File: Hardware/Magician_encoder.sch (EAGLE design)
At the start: 24 parts, among them U1 QRE1113, U2 QRE1113

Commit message: Changed opamp part number to U3
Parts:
- renumbered U$1 to U3
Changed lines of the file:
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@@
 <part name="R1" library="SparkFun-Resistors" deviceset="10KOHM1/10W1%(0603)" device="" value="10k"/>
 <part name="R2" library="SparkFun-Resistors" deviceset="1K-1%" device="" value="1k"/>
-<part name="U$1" library="SparkFun-AnalogIC" deviceset="LMV358" device=""/>
+<part name="U3" library="SparkFun-AnalogIC" deviceset="LMV358" device=""/>
 <part name="U2" library="SparkFun-Sensors" deviceset="QRE1113" device=""/>
 <part name="D1" library="SparkFun-DiscreteSemi" deviceset="RB751" device="" value="RB751"/>
@@
 <instance part="R1" gate="G$1" x="104.14" y="121.92"/>
 <instance part="R2" gate="G$1" x="86.36" y="121.92" rot="R180"/>
-<instance part="U$1" gate="G$1" x="104.14" y="104.14"/>
-<instance part="U$1" gate="G$2" x="200.66" y="104.14"/>
+<instance part="U3" gate="G$1" x="104.14" y="104.14"/>
+<instance part="U3" gate="G$2" x="200.66" y="104.14"/>
 <instance part="U2" gate="G$1" x="48.26" y="109.22" smashed="yes" rot="MR0">
 <attribute name="VALUE" x="50.038" y="112.268" size="1.778" layer="96" rot="MR0"/>
@@
 <segment>
 <pinref part="SUPPLY2" gate="G$1" pin="5V"/>
-<pinref part="U$1" gate="G$1" pin="+V"/>
+<pinref part="U3" gate="G$1" pin="+V"/>
 <wire x1="104.14" y1="111.76" x2="104.14" y2="109.22" width="0.1524" layer="91"/>
 </segment>
@@
 <segment>
 <pinref part="GND2" gate="1" pin="GND"/>
-<pinref part="U$1" gate="G$1" pin="GND"/>
+<pinref part="U3" gate="G$1" pin="GND"/>
 <wire x1="104.14" y1="96.52" x2="104.14" y2="99.06" width="0.1524" layer="91"/>
 </segment>
@@
 <net name="N$1" class="0">
 <segment>
-<pinref part="U$1" gate="G$1" pin="-IN1"/>
+<pinref part="U3" gate="G$1" pin="-IN1"/>
 <wire x1="93.98" y1="106.68" x2="96.52" y2="106.68" width="0.1524" layer="91"/>
 <wire x1="93.98" y1="106.68" x2="93.98" y2="121.92" width="0.1524" layer="91"/>
@@
 <wire x1="109.22" y1="121.92" x2="114.3" y2="121.92" width="0.1524" layer="91"/>
 <wire x1="114.3" y1="121.92" x2="114.3" y2="104.14" width="0.1524" layer="91"/>
-<pinref part="U$1" gate="G$1" pin="OUT1"/>
+<pinref part="U3" gate="G$1" pin="OUT1"/>
 <wire x1="114.3" y1="104.14" x2="111.76" y2="104.14" width="0.1524" layer="91"/>
 <label x="119.38" y="104.14" size="1.778" layer="95" xref="yes"/>
@@
 <net name="N$6" class="0">
 <segment>
-<pinref part="U$1" gate="G$1" pin="+IN1"/>
+<pinref part="U3" gate="G$1" pin="+IN1"/>
 <pinref part="D1" gate="G$1" pin="C"/>
 <wire x1="68.58" y1="99.06" x2="63.5" y2="99.06" width="0.1524" layer="91"/>
@@
 <wire x1="190.5" y1="121.92" x2="187.96" y2="121.92" width="0.1524" layer="91"/>
 <junction x="190.5" y="121.92"/>
-<pinref part="U$1" gate="G$2" pin="-IN2"/>
+<pinref part="U3" gate="G$2" pin="-IN2"/>
 <wire x1="190.5" y1="106.68" x2="193.04" y2="106.68" width="0.1524" layer="91"/>
 </segment>
@@
 <label x="215.9" y="104.14" size="1.778" layer="95" xref="yes"/>
 <wire x1="210.82" y1="104.14" x2="215.9" y2="104.14" width="0.1524" layer="91"/>
-<pinref part="U$1" gate="G$2" pin="OUT2"/>
+<pinref part="U3" gate="G$2" pin="OUT2"/>
 <wire x1="208.28" y1="104.14" x2="210.82" y2="104.14" width="0.1524" layer="91"/>
 <junction x="210.82" y="104.14"/>
@@
 <wire x1="193.04" y1="101.6" x2="160.02" y2="101.6" width="0.1524" layer="91"/>
 <junction x="160.02" y="101.6"/>
-<pinref part="U$1" gate="G$2" pin="+IN2"/>
-</segment>
-</net>
+<pinref part="U3" gate="G$2" pin="+IN2"/>
+</segment>
+</net>

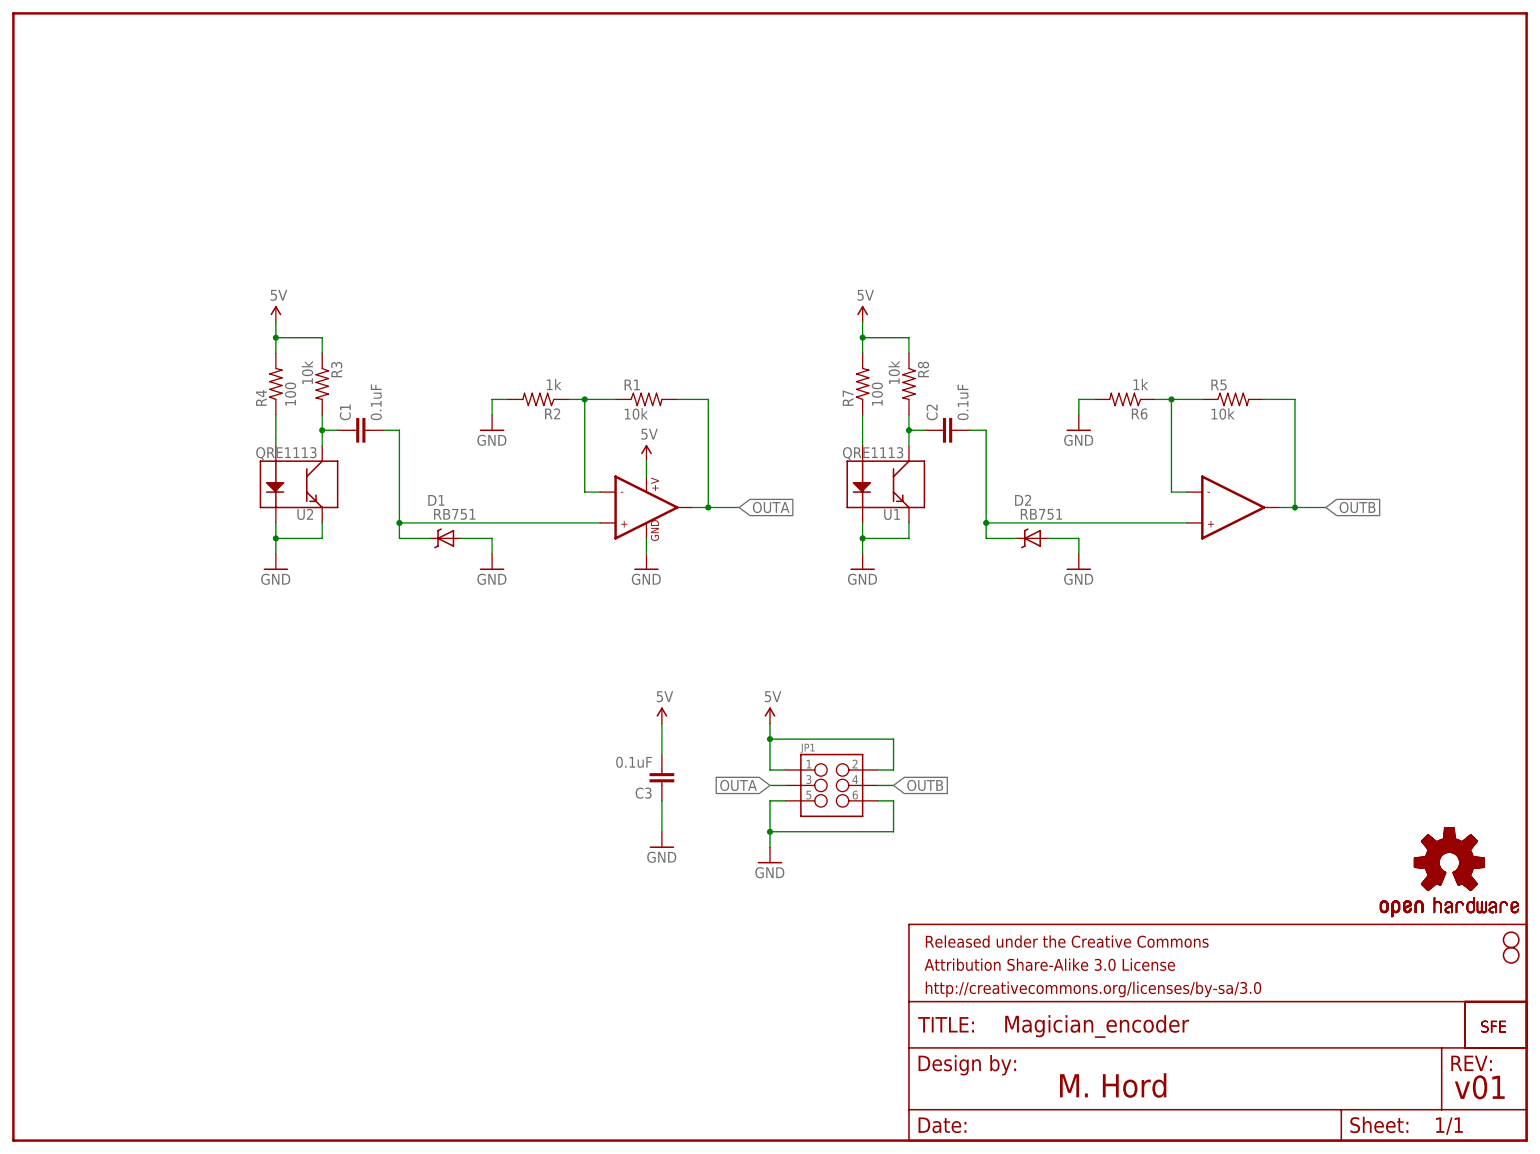
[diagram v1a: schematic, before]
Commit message: Total overhaul to BJT based circuit.
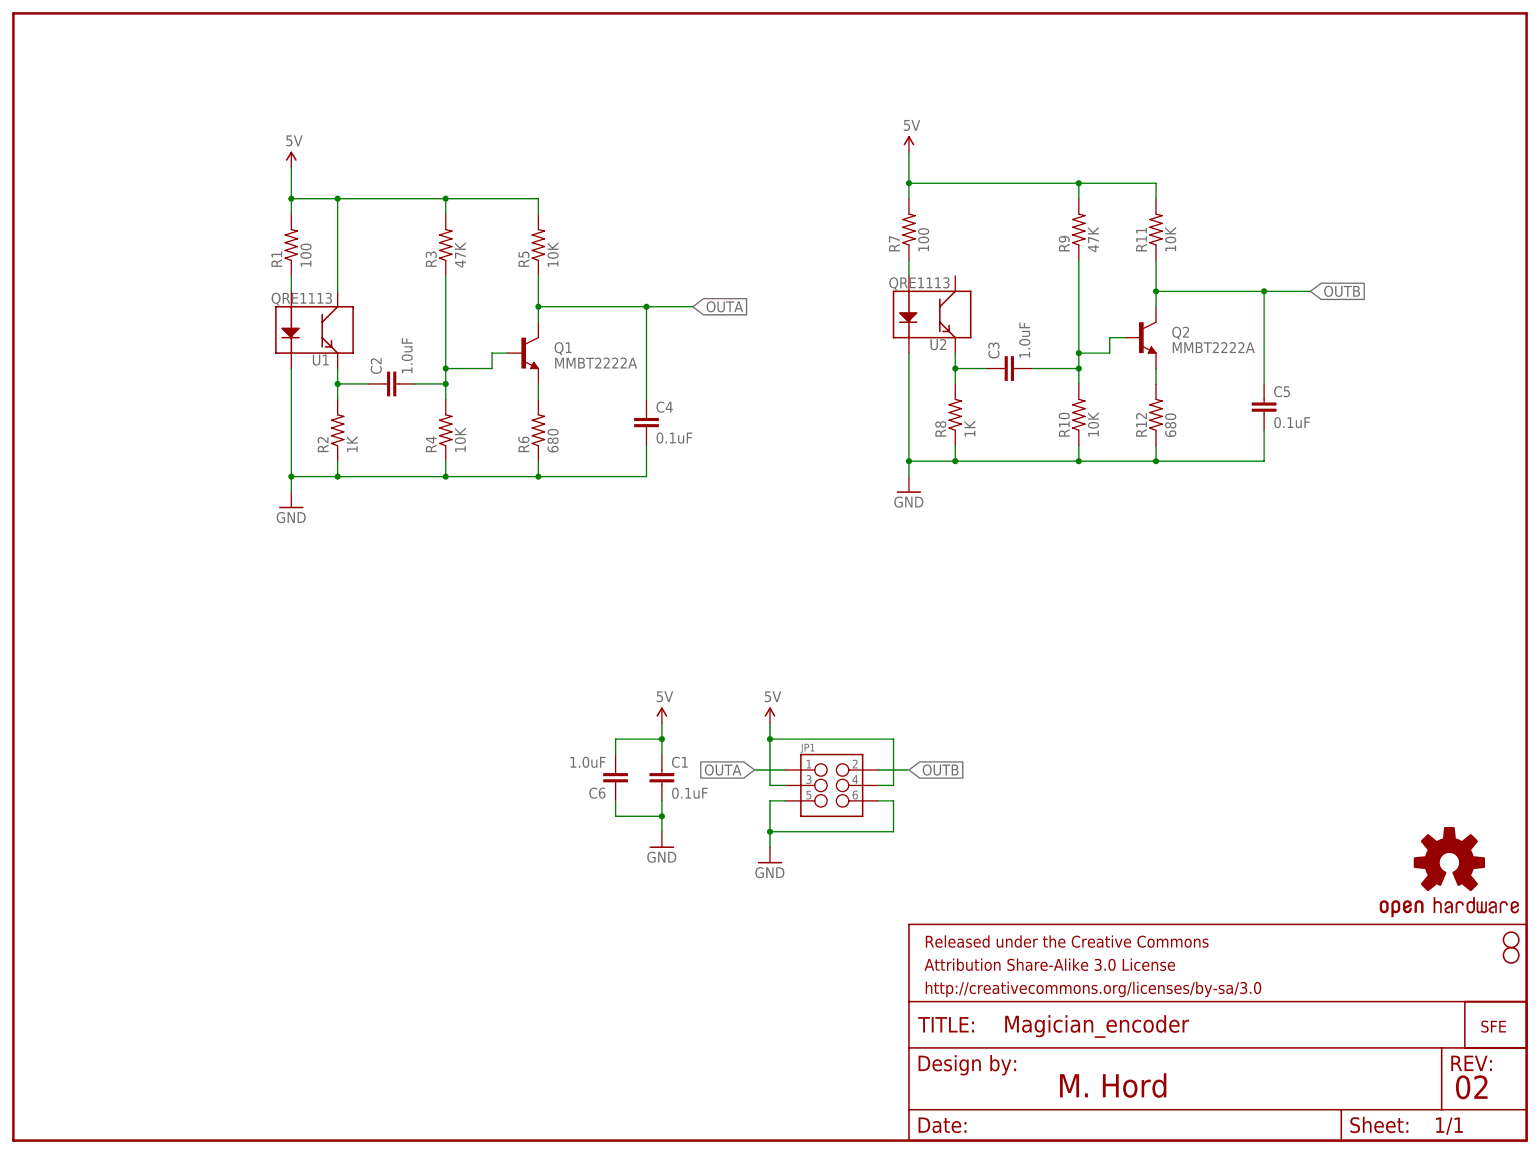
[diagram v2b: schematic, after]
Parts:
- removed D1, D2: RB751, SparkFun-DiscreteSemi:RB751
- removed LOGO1: LOGO-SFENEW, SparkFun-Aesthetics:LOGO-SFENEW
- removed LOGO2: OSHW-LOGOS, SparkFun-Aesthetics:OSHW-LOGOS
- removed U3: LMV358, SparkFun-AnalogIC:LMV358
- added C4, C5: 0.1uF, SparkFun-Capacitors:0.1UF-25V(+80/-20%)(0603)
- added C6: 1.0uF, SparkFun-Capacitors:1.0UF-16V-10%(0603)
- added Q1, Q2: MMBT2222A, SparkFun-DiscreteSemi:TRANSISTOR_NPNMMBT2222A
- added R10, R11: 10K, SparkFun-Resistors:10KOHM1/10W1%(0603)0603
- added R12: 680, SparkFun-Resistors:680OHM1/10W5%(0603)
- added R9: 47K, SparkFun-Resistors:47KOHM1/10W1%(0603)
- C2, C3: value 0.1uF -> 1.0uF; device SparkFun-Capacitors:0.1UF-25V(+80/-20%)(0603) -> SparkFun-Capacitors:1.0UF-16V-10%(0603)
- R1: value 10k -> 100; device SparkFun-Resistors:10KOHM1/10W1%(0603) -> SparkFun-Resistors:100OHM1/10W1%(0603)
- R2: value 1k -> 1K; device SparkFun-Resistors:1K-1% -> SparkFun-Resistors:1KOHM1/10W1%(0603)
- R3: value 10k -> 47K; device SparkFun-Resistors:10KOHM1/10W1%(0603) -> SparkFun-Resistors:47KOHM1/10W1%(0603)
- R4: value 100 -> 10K; device SparkFun-Resistors:100-1% -> SparkFun-Resistors:10KOHM1/10W1%(0603)0603
- R5: value 10k -> 10K; device SparkFun-Resistors:10KOHM1/10W1%(0603) -> SparkFun-Resistors:10KOHM1/10W1%(0603)0603
- R6: value 1k -> 680; device SparkFun-Resistors:1K-1% -> SparkFun-Resistors:680OHM1/10W5%(0603)
- R7: device SparkFun-Resistors:100-1% -> SparkFun-Resistors:100OHM1/10W1%(0603)
- R8: value 10k -> 1K; device SparkFun-Resistors:10KOHM1/10W1%(0603) -> SparkFun-Resistors:1KOHM1/10W1%(0603)
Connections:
- removed net N$11: C2.2, D2.C, U3G$2.+IN2
- removed net N$4: R5.1, R6.1, U3G$2.-IN2
- removed net N$6: C1.2, D1.C, U3G$1.+IN1
- new net N$2: C2.2, Q1.B, R3.1, R4.2
- new net N$7: Q2.E, R12.2
- new net N$8: C3.1, R8.2, U2.E
- net 5V: now also C1.1, C6.2, JP1.3, JP1.4, R1.2, R11.2, R3.2, R5.2, R9.2, U1.C; no longer C3.2, JP1.1, JP1.2, R3.1, R4.2, R8.1, U3G$1.+V
- net GND: now also C1.2, C4.2, C5.2, C6.1, R10.1, R12.1, R2.1, R4.1, R6.1, R8.1; no longer C3.1, D1.A, D2.A, R2.2, R6.2, U1.E, U2.E, U3G$1.GND
- net N$1: now also C2.1, R2.2, U1.E; no longer R1.1, R2.1, U3G$1.-IN1
- net N$10: now also U2.A; no longer U1.A
- net N$3: now also Q1.E, R6.2; no longer C1.1, R3.2, U2.C
- net N$5: now also R1.1, U1.A; no longer R4.1, U2.A
- net N$9: now also C3.2, Q2.B, R10.2, R9.1; no longer C2.1, R8.2, U1.C
- net OUTA: now also C4.1, JP1.1, Q1.C, R5.1; no longer JP1.3, R1.2, U3G$1.OUT1
- net OUTB: now also C5.1, JP1.2, Q2.C, R11.1; no longer JP1.4, R5.2, U3G$2.OUT2
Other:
- note added: "02"
- note removed: "v01"
- moved on the sheet: C1, C2, C3, R1, R2, R3, R4, R5, R6, R7, R8, U1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

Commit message: Change to discrete BJT circuit.
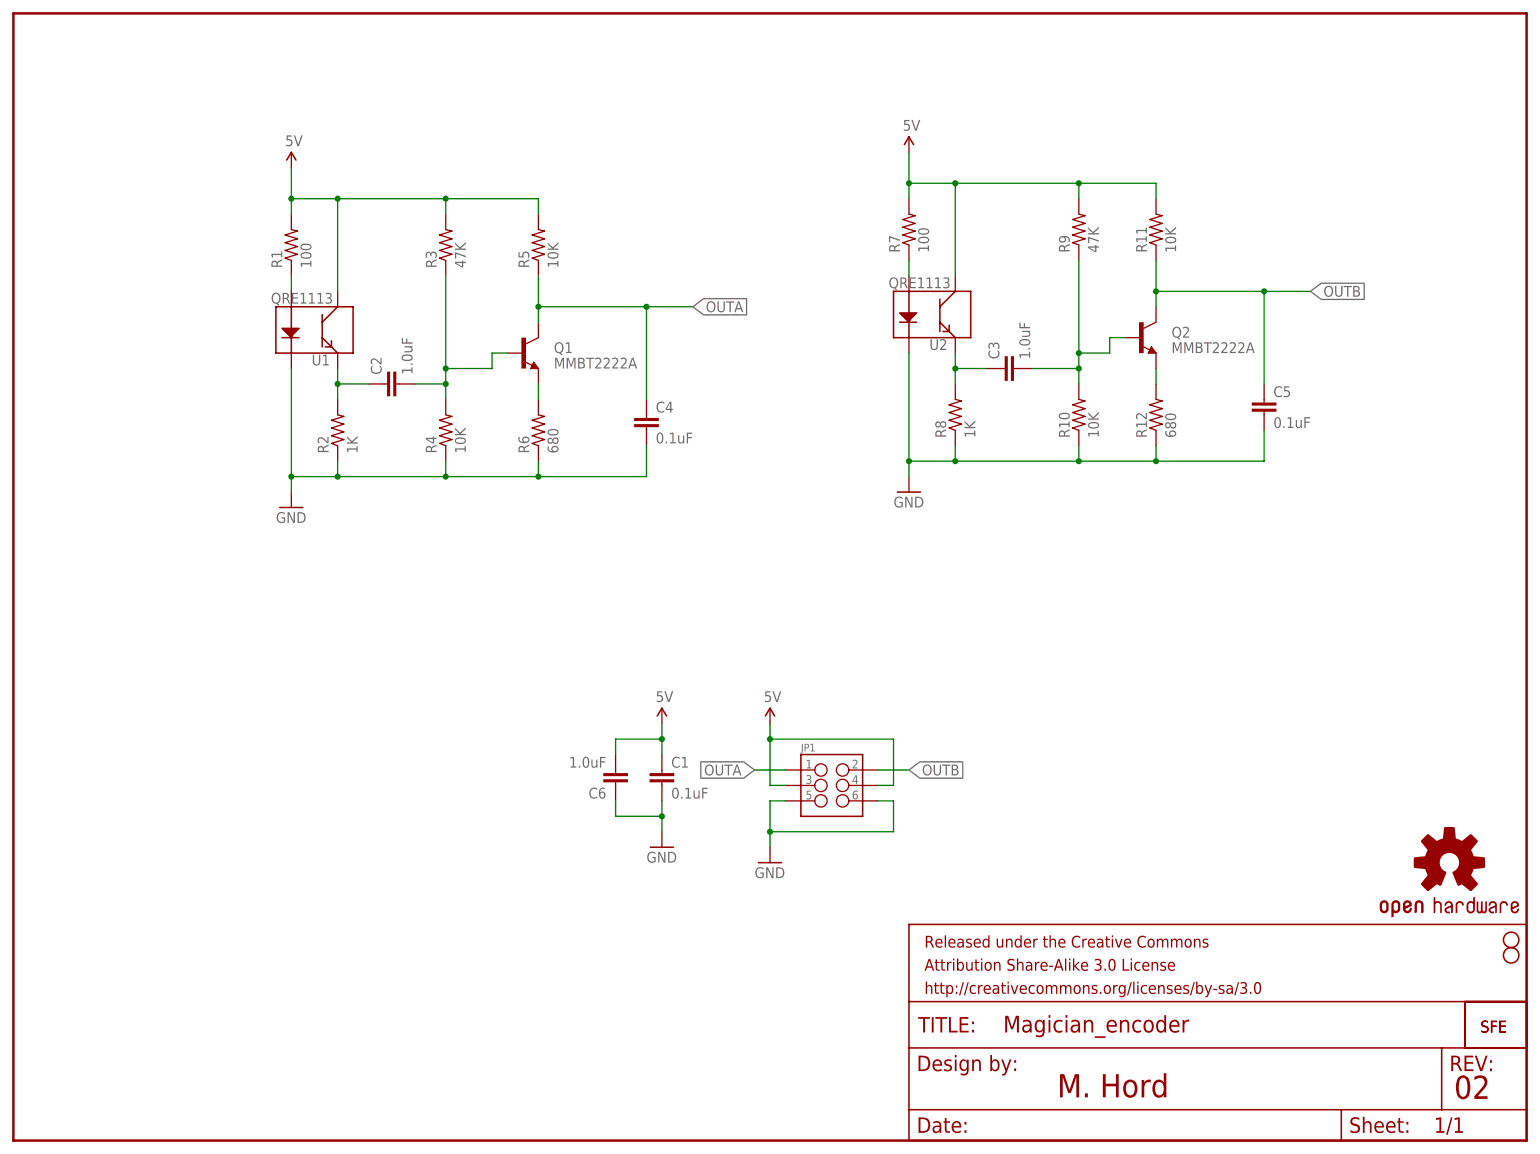
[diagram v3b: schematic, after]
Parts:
- added LOGO1: LOGO-SFESK, SparkFun-Aesthetics:LOGO-SFESK
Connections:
- net 5V: now also U2.C
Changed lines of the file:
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@@
 <part name="Q1" library="SparkFun-DiscreteSemi" deviceset="TRANSISTOR_NPN" device="MMBT2222A" value="MMBT2222A"/>
 <part name="Q2" library="SparkFun-DiscreteSemi" deviceset="TRANSISTOR_NPN" device="MMBT2222A" value="MMBT2222A"/>
+<part name="LOGO1" library="SparkFun-Aesthetics" deviceset="LOGO-SFE" device="SK"/>
 </parts>
 <sheets>
@@
 <instance part="Q1" gate="G$1" x="83.82" y="129.54"/>
 <instance part="Q2" gate="G$1" x="185.42" y="132.08"/>
+<instance part="LOGO1" gate="G$1" x="241.3" y="17.78"/>
 </instances>
 <busses>
@@
 <pinref part="R9" gate="G$1" pin="2"/>
 <wire x1="147.32" y1="157.48" x2="147.32" y2="154.94" width="0.1524" layer="91"/>
-<wire x1="147.32" y1="157.48" x2="175.26" y2="157.48" width="0.1524" layer="91"/>
+<wire x1="147.32" y1="157.48" x2="154.94" y2="157.48" width="0.1524" layer="91"/>
+<wire x1="154.94" y1="157.48" x2="175.26" y2="157.48" width="0.1524" layer="91"/>
 <wire x1="175.26" y1="157.48" x2="175.26" y2="154.94" width="0.1524" layer="91"/>
 <junction x="147.32" y="157.48"/>
@@
 <wire x1="187.96" y1="157.48" x2="187.96" y2="154.94" width="0.1524" layer="91"/>
 <junction x="175.26" y="157.48"/>
+<pinref part="U2" gate="G$1" pin="C"/>
+<wire x1="154.94" y1="142.24" x2="154.94" y2="157.48" width="0.1524" layer="91"/>
+<junction x="154.94" y="157.48"/>
 </segment>
 <segment>
